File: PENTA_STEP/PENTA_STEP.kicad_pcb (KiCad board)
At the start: 4 copper layers, 200 x 100 mm, 359 parts, among them J1 DB25_Female_LCNC, J10 ENC_HEADER, J11 ENC_HEADER, J12 PSoC_PROG, J14 SCREW TERM, J15 SCREW TERM, J16 ENC_HEADER, J17 ENC_HEADER, J18 SCREW TERM, J19 SCREW TERM, J2 MTA-100, J20 CYP_I2C, J3 USB_B, J4 SPARE_IN, J5 ENC_HEADER, J6 Conn_02x02_Odd_Even, J7 CYP_GPIO, J8 ICSP, J9 SCREW TERM, Q1 BUK9K45-100E,115, Q10 BUK9K45-100E,115, Q11 BUK9K45-100E,115, Q12 BUK9K45-100E,115, Q13 BUK9K45-100E,115, Q14 BUK9K45-100E,115, Q15 BUK9K45-100E,115, Q16 BUK9K45-100E,115, Q17 BUK9K45-100E,115, Q18 BUK9K45-100E,115, Q19 BUK9K45-100E,115, Q2 BUK9K45-100E,115, Q20 BUK9K45-100E,115, Q3 BUK9K45-100E,115, Q4 BUK9K45-100E,115, Q5 BUK9K45-100E,115, Q6 BUK9K45-100E,115, Q7 BUK9K45-100E,115, Q8 BUK9K45-100E,115, Q9 BUK9K45-100E,115, U1 14S1, U2 TQFP-100, U3 eTQFP48_9x9, U4 eTQFP48_9x9, U5 eTQFP48_9x9, U6 eTQFP48_9x9, U7 eTQFP48_9x9, Y1 10MHz

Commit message: progressing on layout
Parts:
- C23, C29, Q3, Q4, R102: moved to B.Cu
- C27, C28, R103, R104, R98, R99: moved to F.Cu
- moved C37 20.9 mm to (142.7, 58.9)
- moved C38 20.9 mm to (138.6, 58.9)
- moved C39 20.9 mm to (147.5, 58.9)
- moved R104 16.9 mm to (128.9, 67.4)
- moved C29 15.9 mm to (118.2, 51.7), turned to 90 degrees
- moved C24 15.4 mm to (131.4, 51.7), turned to 90 degrees
- moved R99 15.1 mm to (123.0, 67.4)
- moved C25 12.2 mm to (123.2, 76.5)
- moved C26 12.2 mm to (121.9, 79.8)
- moved TP1 12.2 mm to (107.9, 82.8)
- moved U3 12.2 mm to (114.3, 77.7)
- moved C18 12.2 mm to (105.4, 76.5), turned to 90 degrees
- moved C31 12.1 mm to (130.0, 61.2)
- moved C30 12.1 mm to (123.7, 61.2)
- moved Q3 11.9 mm to (124.9, 61.0)
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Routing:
- net /DRIVE_1/BMB2: track 0.00 -> 18.7 mm, vias 0 -> 6
- net GND: track 7.47 -> 24.6 mm, vias 0 -> 20
- net Net-(Q3-Pad3): track 0.00 -> 16.3 mm
- net /DRIVE_1/BMB1: track 0.00 -> 14.6 mm, vias 0 -> 6
- net /DRIVE_1/VM: track 0.00 -> 6.77 mm, vias 0 -> 38
- net /DRIVE_1/BMA2: track 9.65 -> 14.9 mm, vias 0 -> 6
- net /DRIVE_1/BMA1: track 11.0 -> 15.5 mm, vias 0 -> 6
- net Net-(Q4-Pad4): track 0.00 -> 2.70 mm, vias 0 -> 1
- net Net-(Q4-Pad2): track 0.00 -> 2.44 mm, vias 0 -> 1
- net Net-(Q2-Pad4): track 0.00 -> 2.44 mm, vias 0 -> 1
- net Net-(Q2-Pad2): track 0.00 -> 2.44 mm, vias 0 -> 1
- net Net-(Q3-Pad4): track 0.00 -> 2.31 mm, vias 0 -> 1
- net Net-(Q3-Pad2): track 0.00 -> 2.31 mm, vias 0 -> 1
- net Net-(Q1-Pad4): track 0.00 -> 2.31 mm, vias 0 -> 1
- net Net-(Q1-Pad2): track 0.00 -> 2.31 mm, vias 0 -> 1
- added copper zone on B.Cu, net /DRIVE_1/BMA1
- added copper zone on F.Cu, net /DRIVE_1/BMA1
- added copper zone on B.Cu, net /DRIVE_1/BMA2
- added copper zone on F.Cu, net /DRIVE_1/BMA2
- added copper zone on B.Cu, net /DRIVE_1/BMB1
- added copper zone on F.Cu, net /DRIVE_1/BMB1
- added copper zone on B.Cu, net /DRIVE_1/BMB2
- added copper zone on F.Cu, net /DRIVE_1/BMB2
- added copper zone on B.Cu, net /DRIVE_1/VM
- added copper zone on GND1.Cu, net GND
- added copper zone on GND2.Cu, net GND
- added copper zone on B.Cu, net Net-(F1-Pad3)
- removed copper zone on POWER.Cu, net Net-(F1-Pad3)
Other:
- board text added: "1"
- board text added: "10"
- board text added: "2"
- board text added: "3"
- board text added: "4"
- board text added: "PP15 PP10 PP11 PP12 PP13"
- board text added: "PP17"
- board text added: "SPARE IN"

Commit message: V1 layout nearing completion
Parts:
- C1, C10, C100, C11, C12, C13, C14, C15, C2, C23, C24, C25, C26, C27, C28, C29, C3, C30, C31, C32, C4, C40, C43, C44, C45, C49, C58, C6, C60, C61, C62, C66, C74, C77, C78, C79, C8, C83, C9, C91, C94, C95, C96: footprint Capacitor_SMD:C_0603_1608Metric -> Capacitor_SMD:C_0603_1608Metric_Pad1.05x0.95mm_HandSolder
- C34, C52, C69, C86, R117, R118, R122, R123, R136, R137, R141, R142, R155, R156, R160, R161, R20, R21, R25, R26: moved to F.Cu
- C41, C46, C57, C63, C75, C80, C92, C97: footprint Capacitor_SMD:C_0603_1608Metric -> Capacitor_SMD:C_0603_1608Metric_Pad1.05x0.95mm_HandSolder; moved to B.Cu
- C42, C47, C48, C59, C64, C65, C76, C81, C82, C93, C98, C99: footprint Capacitor_SMD:C_0603_1608Metric -> Capacitor_SMD:C_0603_1608Metric_Pad1.05x0.95mm_HandSolder; moved to F.Cu
- JP19, JP38, JP74, JP76, JP98, Q11, Q12, Q15, Q16, Q19, Q20, Q7, Q8, R100, R101, R106, R108, R11, R112, R113, R119, R120, R121, R125, R127, R131, R132, R140, R144, R146, R15, R150, R151, R159, R16, R24, R4, R87, R89, R90, R93, R94: moved to B.Cu
- U1: value 14S1 -> ATTINY841-SSU
- U2: value TQFP-100 -> CY8C5468AXI-LP106
- U3, U4, U5, U6, U7: value eTQFP48_9x9 -> TMC5160-TA
- moved J10 40.3 mm to (87.1, 83.1), turned to 90 degrees
- moved J17 39.5 mm to (197.1, 115.8), turned to 270 degrees
- moved J5 39.4 mm to (124.2, 115.8), turned to 270 degrees
- moved R133 36.8 mm to (225.3, 132.1), turned to 0 degrees
- moved R132 36.8 mm to (216.4, 125.7)
- moved J11 36.7 mm to (156.4, 83.1), turned to 90 degrees
- moved R131 36.4 mm to (214.8, 125.7)
- moved JP17 35.3 mm to (89.6, 79.8)
- moved C19 34.6 mm to (134.5, 80.4), turned to 270 degrees
- moved R128 34.5 mm to (220.6, 124.5), turned to 45 degrees
- moved JP72 34.4 mm to (194.5, 119.1)
- moved JP96 34.3 mm to (121.6, 119.1)
- moved R17 34.0 mm to (74.4, 129.0), turned to 270 degrees
- moved J16 34.0 mm to (212.1, 82.3), turned to 0 degrees
- moved R16 33.8 mm to (80.7, 120.1)
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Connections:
- J14 pad 3: /DRIVE_1/BMA1 -> /DRIVE_1/BMB1
- J14 pad 4: /DRIVE_1/BMA2 -> /DRIVE_1/BMB2
- J14 pad 5: /DRIVE_1/BMB1 -> /DRIVE_1/BMA1
- J14 pad 6: /DRIVE_1/BMB2 -> /DRIVE_1/BMA2
- J15 pad 3: /DRIVE_2/BMA1 -> /DRIVE_2/BMB1
- J15 pad 4: /DRIVE_2/BMA2 -> /DRIVE_2/BMB2
- J15 pad 5: /DRIVE_2/BMB1 -> /DRIVE_2/BMA1
- J15 pad 6: /DRIVE_2/BMB2 -> /DRIVE_2/BMA2
- J18 pad 3: /DRIVE_3/BMA1 -> /DRIVE_3/BMB1
- J18 pad 4: /DRIVE_3/BMA2 -> /DRIVE_3/BMB2
- J18 pad 5: /DRIVE_3/BMB1 -> /DRIVE_3/BMA1
- J18 pad 6: /DRIVE_3/BMB2 -> /DRIVE_3/BMA2
- J19 pad 3: /DRIVE_4/BMA1 -> /DRIVE_4/BMB1
- J19 pad 4: /DRIVE_4/BMA2 -> /DRIVE_4/BMB2
- J19 pad 5: /DRIVE_4/BMB1 -> /DRIVE_4/BMA1
- J19 pad 6: /DRIVE_4/BMB2 -> /DRIVE_4/BMA2
- J9 pad 3: /DRIVE_5/BMA1 -> /DRIVE_5/BMB1
- J9 pad 4: /DRIVE_5/BMA2 -> /DRIVE_5/BMB2
- J9 pad 5: /DRIVE_5/BMB1 -> /DRIVE_5/BMA1
- J9 pad 6: /DRIVE_5/BMB2 -> /DRIVE_5/BMA2
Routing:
- net GND: track 24.6 -> 392.3 mm, vias 20 -> 305
- net /DRIVE_4/~DRV_ENN: track 0.00 -> 49.3 mm, vias 0 -> 1
- net /DRIVE_3/~DRV_ENN: track 0.00 -> 49.3 mm, vias 0 -> 1
- net /DRIVE_1/~DRV_ENN: track 0.00 -> 49.3 mm, vias 0 -> 1
- net /DRIVE_5/~DRV_ENN: track 0.00 -> 49.3 mm, vias 0 -> 1
- net /DRIVE_2/~DRV_ENN: track 0.00 -> 49.3 mm, vias 0 -> 1
- net /DRIVE_2/ENC_N: track 0.00 -> 46.8 mm
- net /DRIVE_1/ENC_N: track 0.00 -> 46.8 mm
- net /DRIVE_4/ENC_N: track 0.00 -> 46.8 mm
- net /DRIVE_5/ENC_N: track 0.00 -> 46.8 mm
- net /DRIVE_3/ENC_N: track 0.00 -> 46.8 mm
- net /DRIVE_3/VM: track 0.00 -> 45.5 mm, vias 0 -> 46
- net /DRIVE_2/VM: track 0.00 -> 45.5 mm, vias 0 -> 46
- net /DRIVE_5/VM: track 0.00 -> 45.5 mm, vias 0 -> 46
- net /DRIVE_4/VM: track 0.00 -> 45.5 mm, vias 0 -> 46
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- added copper zone on B.Cu, net /DRIVE_2/VM
- added copper zone on F.Cu, net /DRIVE_2/VM
- added copper zone on B.Cu, net /DRIVE_3/VM
- added copper zone on F.Cu, net /DRIVE_3/VM
- added copper zone on B.Cu, net /DRIVE_4/VM
- added copper zone on F.Cu, net /DRIVE_4/VM
- added copper zone on B.Cu, net /DRIVE_5/VM
- added copper zone on F.Cu, net /DRIVE_5/VM
- added copper zone on B.Cu, net Net-(F2-Pad3)
- added copper zone on B.Cu, net Net-(F3-Pad3)
- added copper zone on B.Cu, net Net-(F4-Pad3)
- added copper zone on B.Cu, net Net-(F5-Pad3)
- added copper zone on B.Cu, net Net-(Q1-Pad3)
- added copper zone on B.Cu, net Net-(Q10-Pad3)
- added copper zone on B.Cu, net Net-(Q11-Pad3)
- added copper zone on B.Cu, net Net-(Q13-Pad3)
- added copper zone on B.Cu, net Net-(Q15-Pad3)
- added copper zone on B.Cu, net Net-(Q17-Pad3)
- added copper zone on B.Cu, net Net-(Q19-Pad3)
- added copper zone on B.Cu, net Net-(Q3-Pad3)
- added copper zone on B.Cu, net Net-(Q5-Pad3)
- added copper zone on B.Cu, net Net-(Q7-Pad3)
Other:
- net class Default: clearance 0.2 -> 0.127
- rule trace_clearance: 0.2 -> 0.127
- rule trace_min: 0.2 -> 0.0889

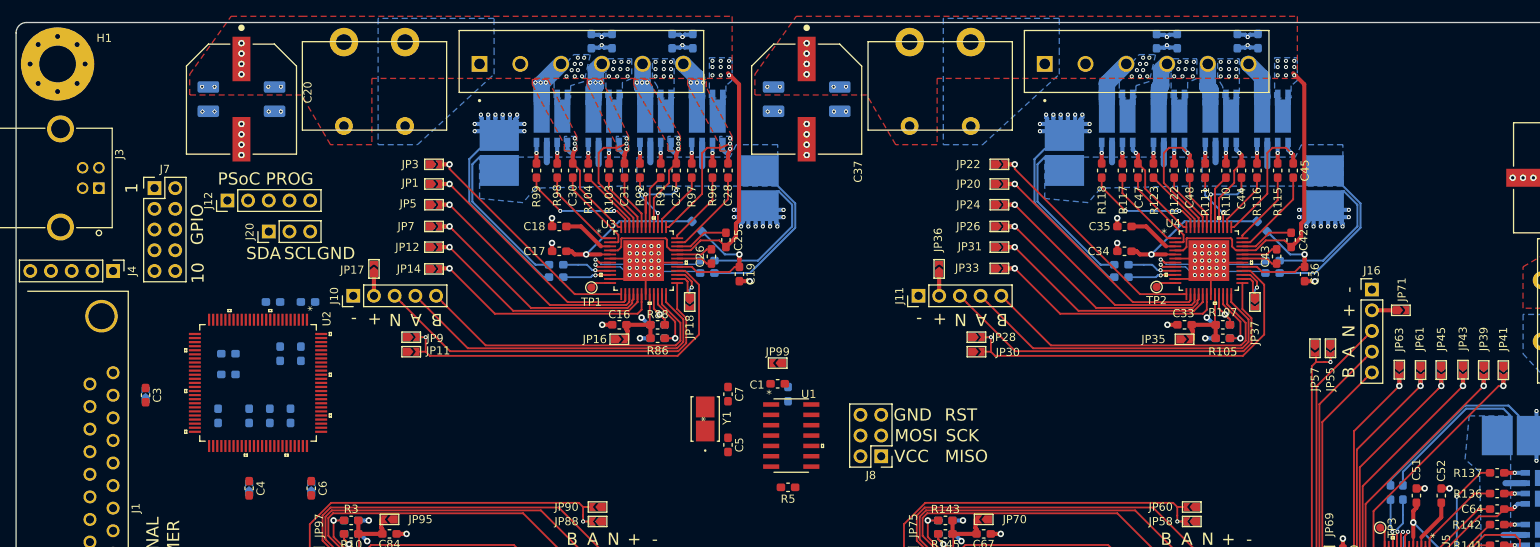
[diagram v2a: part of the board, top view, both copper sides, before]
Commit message: Added two FET-controlled outputs to the board
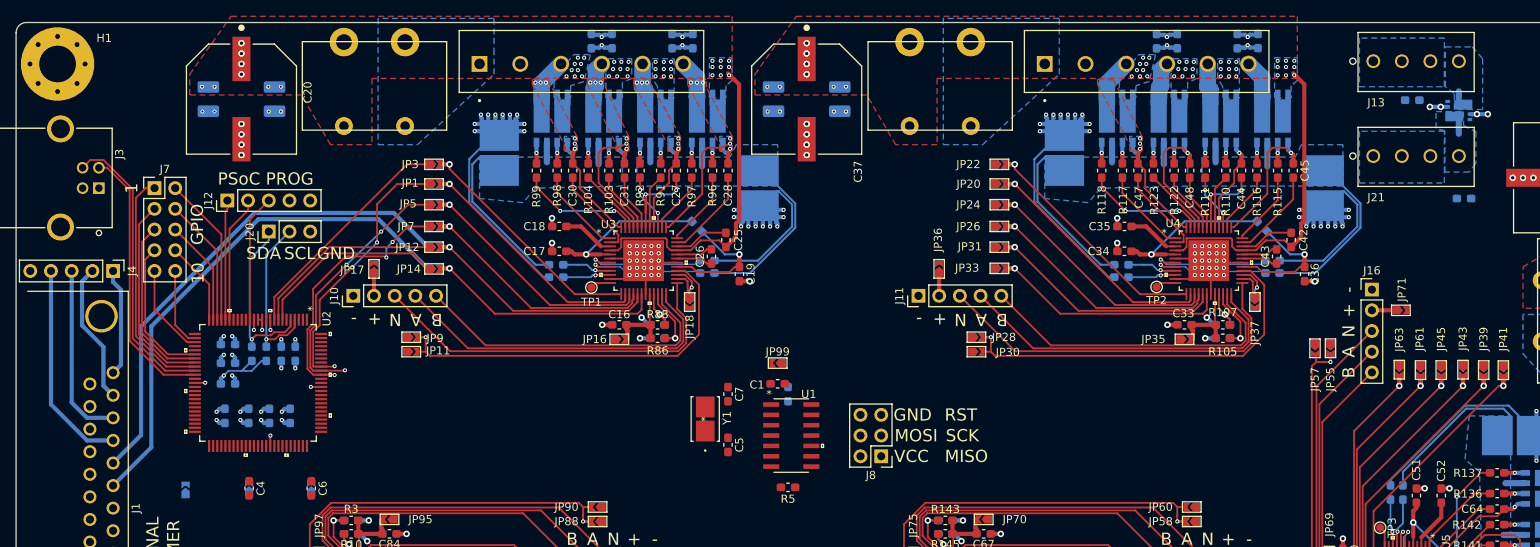
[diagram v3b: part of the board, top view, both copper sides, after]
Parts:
- added J13: PWR_SW_CH1, CUSTOM_FP:1776275-4, F.Cu at (222.7, 54.3)
- added J21: PWR_SW_CH2, CUSTOM_FP:1776275-4, F.Cu at (222.7, 65.9)
- added Q21: AON7804, CUSTOM_FP:DFN3X3_AON7804, B.Cu at (222.7, 60.3)
- added R1: 2R2, Resistor_SMD:R_0603_1608Metric_Pad1.05x0.95mm_HandSolder, B.Cu at (217.0, 59.1)
- added R2: 2R2, Resistor_SMD:R_0603_1608Metric_Pad1.05x0.95mm_HandSolder, B.Cu at (223.4, 71.1)
- C3: moved to B.Cu
- moved JP77 12.6 mm to (66.5, 106.9)
- moved C3 10.2 mm to (71.7, 93.9), turned to 0 degrees
- moved R163 8.16 mm to (76.4, 90.2), turned to 90 degrees
- moved R162 6.87 mm to (74.6, 90.2), turned to 90 degrees
- moved C13 1.39 mm to (71.7, 91.3)
- moved C9 1.14 mm to (71.7, 89.0)
- moved C11 0.84 mm to (71.3, 97.8)
- moved C10 0.69 mm to (80.0, 90.2)
- moved C15 0.14 mm to (78.3, 90.2)
- moved C12 0.05 mm to (74.3, 97.8)
- moved C14 0.05 mm to (76.8, 97.8)
- moved C8 0.05 mm to (79.3, 97.8)
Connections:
- J1 pad 14: /PAR_STEP5 -> /PAR_DIR5
- J1 pad 16: /PAR_DIR5 -> /PAR_STEP4
- J1 pad 2: /PAR_STEP1 -> /PAR_STEP5
- J1 pad 3: /PAR_DIR1 -> /PAR_DIR4
- J1 pad 4: /PAR_STEP2 -> /PAR_DIR3
- J1 pad 5: /PAR_DIR2 -> /PAR_STEP3
- J1 pad 6: /PAR_STEP3 -> /PAR_DIR2
- J1 pad 7: /PAR_DIR3 -> /PAR_STEP2
- J1 pad 8: /PAR_STEP4 -> /PAR_DIR1
- J1 pad 9: /PAR_DIR4 -> /PAR_STEP1
- U2 pad 22: Net-(J7-Pad1) -> Net-(J7-Pad2)
- U2 pad 23: Net-(J7-Pad2) -> Net-(J7-Pad4)
- U2 pad 24: Net-(J7-Pad3) -> Net-(J7-Pad6)
- U2 pad 25: Net-(J7-Pad4) -> Net-(J7-Pad8)
- U2 pad 27: Net-(J7-Pad5) -> Net-(J7-Pad10)
- U2 pad 28: Net-(J7-Pad6) -> Net-(J7-Pad9)
- U2 pad 32: Net-(J7-Pad8) -> Net-(J7-Pad5)
- U2 pad 33: Net-(J7-Pad9) -> Net-(J7-Pad3)
- U2 pad 34: Net-(J7-Pad10) -> Net-(J7-Pad1)
- U2 pad 7: Net-(U2-Pad7) -> /CYP_DIR1
- U2 pad 8: Net-(U2-Pad8) -> /CYP_STEP1
- U2 pad 84: /CYP_DIR1 -> /PWR_SW_CH2
- U2 pad 85: /CYP_STEP1 -> /PWR_SW_CH1
- U2 pad 9: Net-(U2-Pad9) -> /CYP_CS1
- U2 pad 99: /CYP_CS1 -> Net-(U2-Pad99)
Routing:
- net /PAR_DIR1: track 0.00 -> 63.4 mm
- net /PAR_STEP1: track 0.00 -> 60.9 mm
- net /USBIO_D+: track 0.00 -> 35.6 mm
- net /USBIO_D-: track 0.00 -> 33.1 mm
- net /CYP_SCK: track 0.00 -> 33.1 mm, vias 0 -> 3
- net /CYP_MOSI: track 0.00 -> 31.9 mm, vias 0 -> 3
- net /CYP_MISO: track 0.00 -> 31.8 mm, vias 0 -> 3
- net Net-(J7-Pad1): track 0.00 -> 28.5 mm
- net /CYP_CS1: track 0.00 -> 28.4 mm
- net Net-(J1-Pad10): track 0.00 -> 25.8 mm
- net Net-(J7-Pad3): track 0.00 -> 24.5 mm
- net /CYP_STEP1: track 0.00 -> 23.6 mm
- net /CYP_DIR1: track 0.00 -> 23.5 mm
- net Net-(J1-Pad11): track 0.00 -> 22.0 mm
- net /CYP_SDA: track 0.00 -> 21.4 mm, vias 0 -> 1
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- added copper zone on B.Cu, net /DRIVE_2/BMB1
- added copper zone on B.Cu, net Net-(J13-Pad1)
- added copper zone on B.Cu, net Net-(J13-Pad4)
- added copper zone on B.Cu, net Net-(J21-Pad1)
- added copper zone on B.Cu, net Net-(J21-Pad4)
